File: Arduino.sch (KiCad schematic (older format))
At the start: 13 parts, among them U1 DS1337_AH, U2 24LC1025, U3 24LC1025, U4 ATMEGA328P-AU, Y1 Crystal 32MHZ, Y2 Crystal 16MHZ

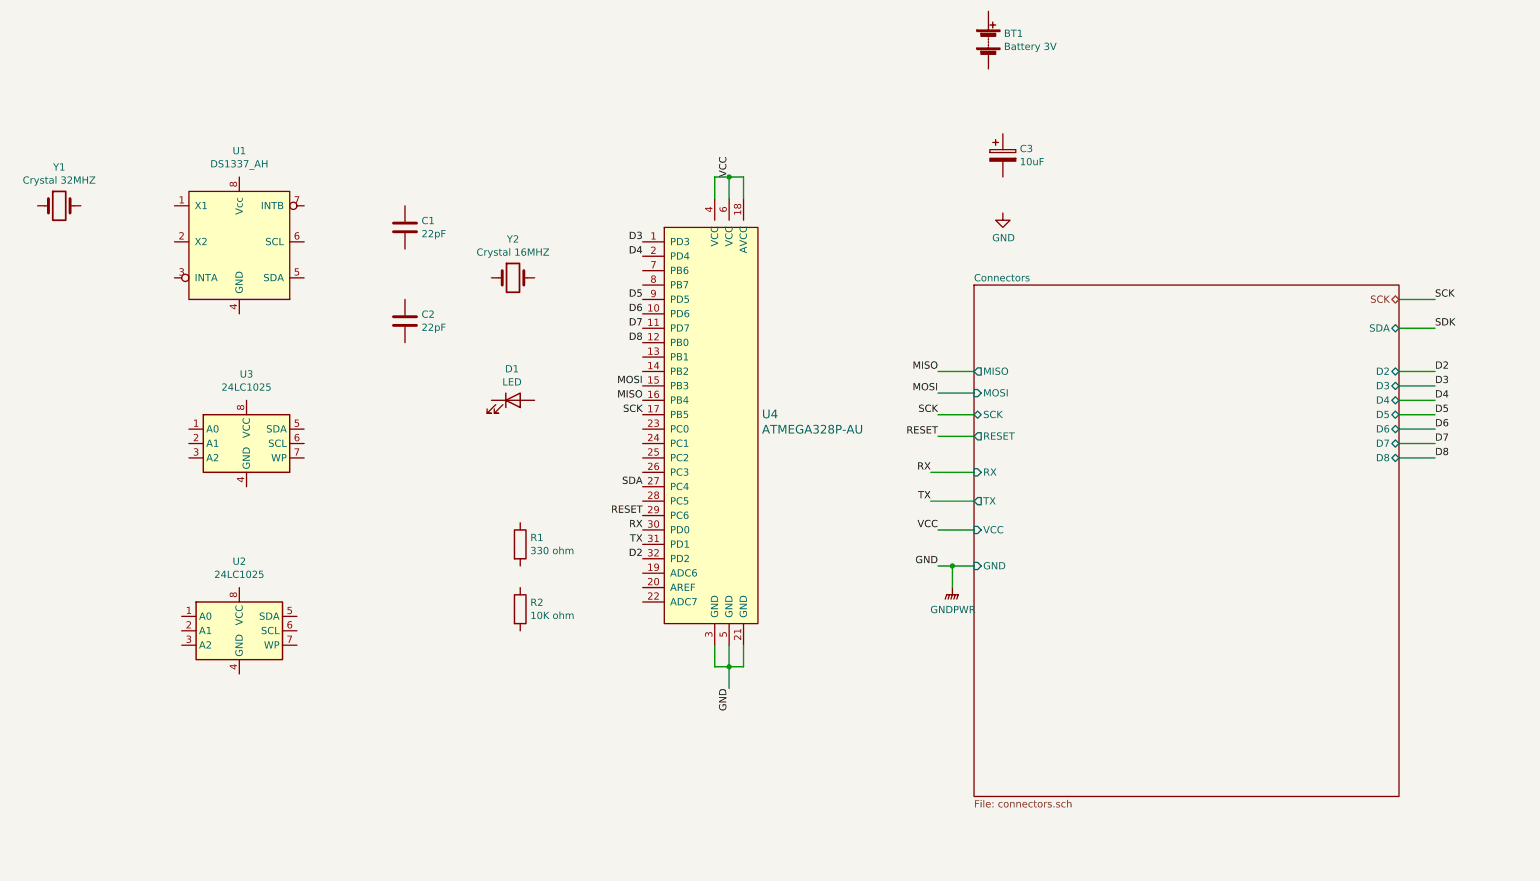
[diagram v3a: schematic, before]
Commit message: Generate a netList
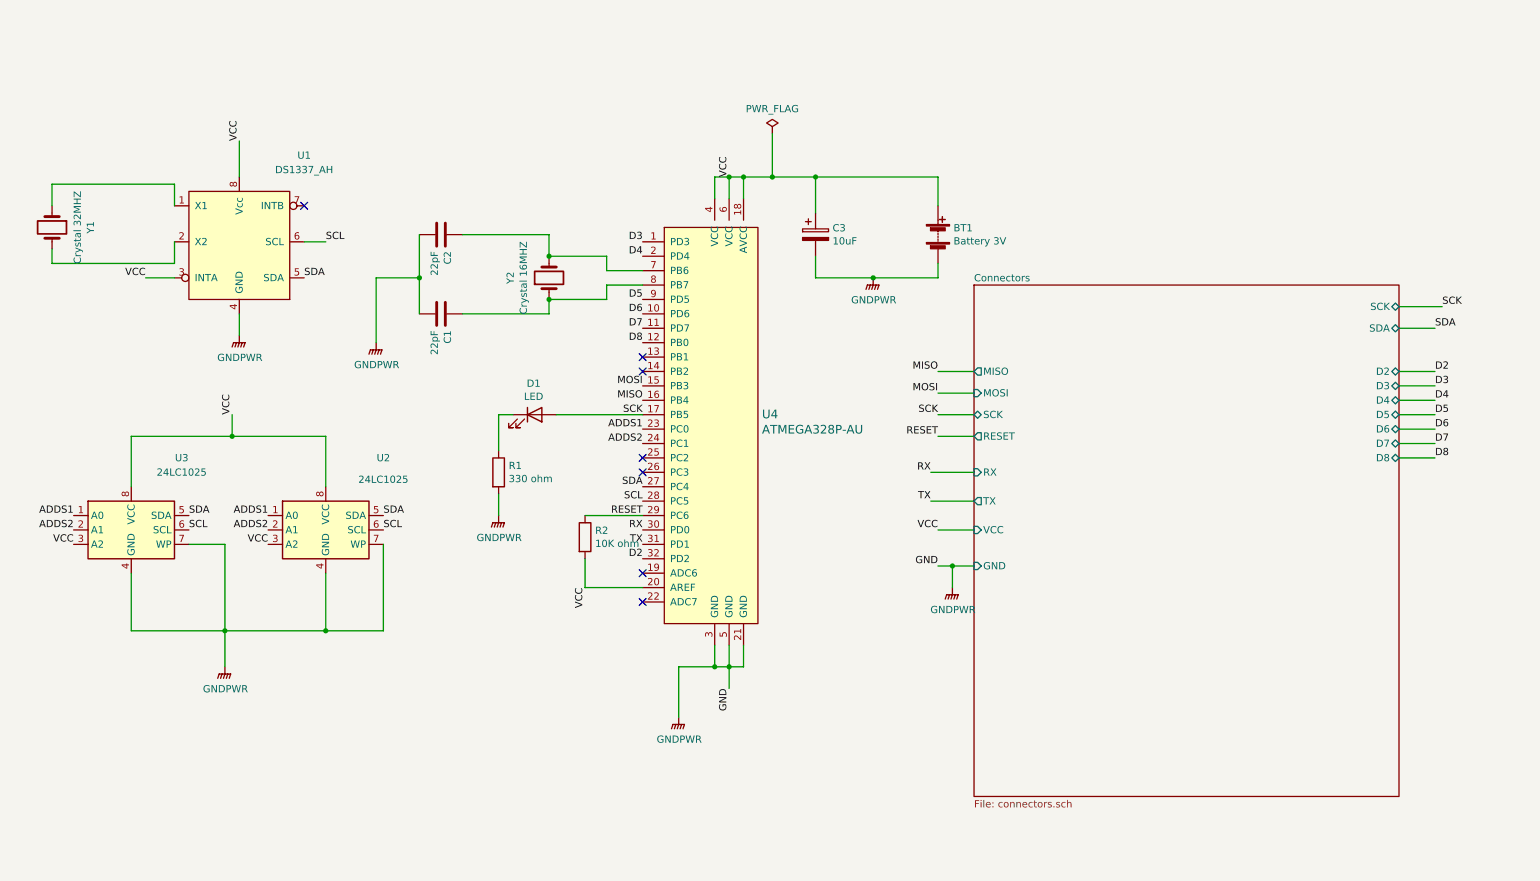
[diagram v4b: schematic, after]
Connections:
- net GND is gone; now on net GNDPWR: U4.21 (GND), U4.3 (GND), U4.5 (GND)
- net RESET: now also R2.1
- net SCK: now also D1.2 (A)
- net SDA: now also U1.5 (SDA), U2.5 (SDA), U3.5 (SDA)
- net VCC: now also BT1.1 (+), C3.1, R2.2, U1.3 (INTA), U1.8 (Vcc), U2.3 (A2), U2.8 (VCC), U3.3 (A2), U3.8 (VCC), U4.20 (AREF)
- net GNDPWR: now reaches BT1.2 (-)
- net GNDPWR: now also C1.2, C2.2, C3.2, R1.2, U1.4 (GND), U2.4 (GND), U2.7 (WP), U3.4 (GND), U3.7 (WP)
- net at C1.1: now also U4.8 (PB7), Y2.1
- net at C2.1: now also U4.7 (PB6), Y2.2
- net at D1.1 (K): now also R1.1
- net ADDS1: now reaches U3.1 (A0)
- net ADDS1: now also U2.1 (A0), U4.23 (PC0)
- net ADDS2: now reaches U3.2 (A1)
- net ADDS2: now also U2.2 (A1), U4.24 (PC1)
- net SCL: now reaches U3.6 (SCL)
- net SCL: now also U1.6 (SCL), U2.6 (SCL), U4.28 (PC5)
- net at U1.1 (X1): now also Y1.1
- net at U1.2 (X2): now also Y1.2
- no-connect marks 0 -> 7
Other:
- moved on the sheet: BT1, C1, C2, C3, D1, R1, R2, U2, U3, Y1, Y2
